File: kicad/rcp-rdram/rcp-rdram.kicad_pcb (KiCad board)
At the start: 2 copper layers, 47.1 x 49.7 mm, 32 parts, among them P1 RDRAM-EDGE, U11 RDRAM18-NUS, U11-2 RDRAM18-NUS, U14 RDRAM18-NUS, U14-2 RDRAM18-NUS, U15 MX8330, X2 14.705MHz

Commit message: Adjusted HC49 crystal to local footprint copy
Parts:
- X2: footprint Crystals:HC-49V -> n64:Crystal_HC-49V
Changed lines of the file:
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@@
       (net 2 GND) (zone_connect 1))
   )
-  (module Crystals:HC-49V (layer B.Cu)
+  (module n64:Crystal_HC-49V (layer B.Cu)
     (at 60.966 61.341 180)
     (descr "Quartz boitier HC-49 Vertical")

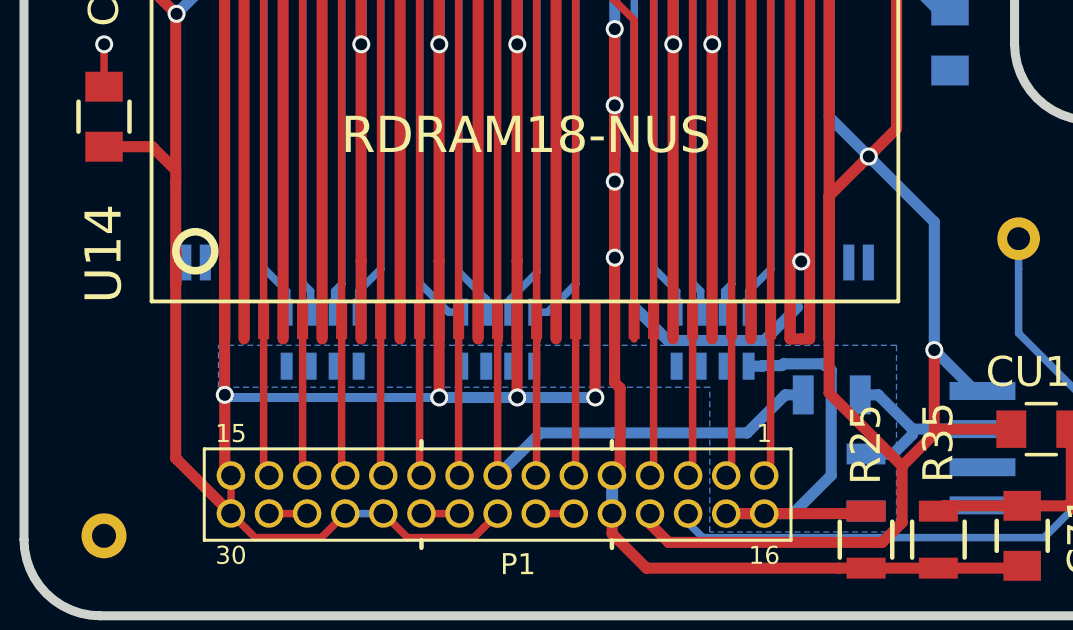
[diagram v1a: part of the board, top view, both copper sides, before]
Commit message: VTERM decouple capacitors added
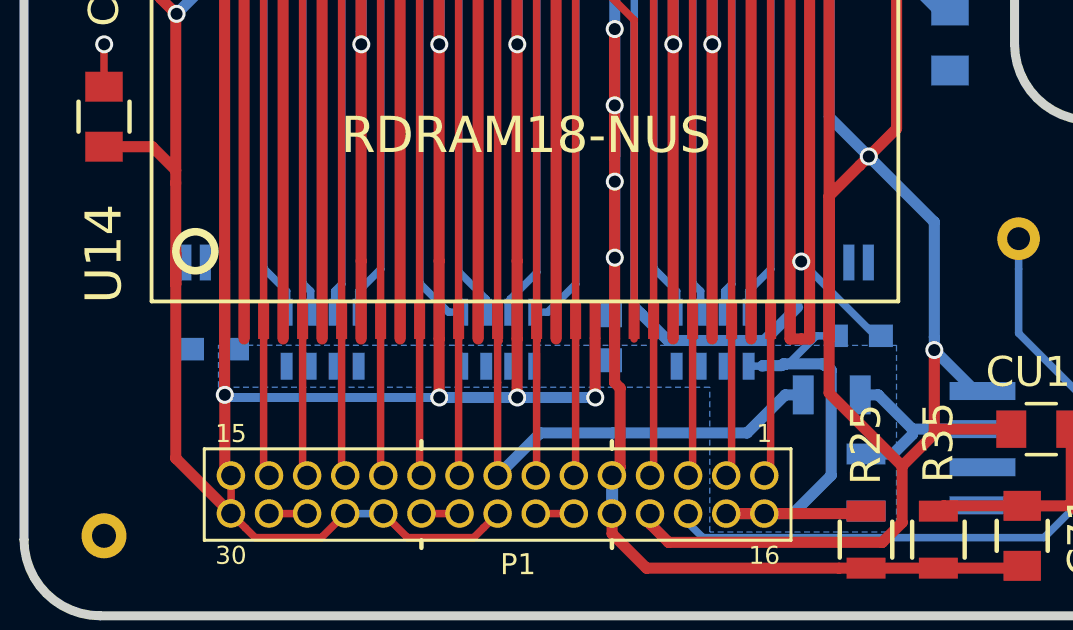
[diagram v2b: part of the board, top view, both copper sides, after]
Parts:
- added C1: 100nF, Capacitors_SMD:C_0603, B.Cu at (29.1, 65.0)
- added C2: 100nF, n64:C_0603, B.Cu at (42.3, 64.6)
- added C3: 100nF, n64:C_0603, B.Cu at (50.5, 64.6)
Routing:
- net GND: track 677.8 -> 681.4 mm
- net /VTERM: track 15.1 -> 18.0 mm
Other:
- board text added: "15"
- board text added: "30"
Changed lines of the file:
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@@
-(kicad_pcb (version 4) (host pcbnew 4.0.5)
+(kicad_pcb (version 4) (host pcbnew 4.0.6)
   (general
-    (links 203)
+    (links 209)
     (no_connects 0)
     (area 22.582999 24.105399 70.000001 74.062401)
     (thickness 1.6)
-    (drawings 25)
-    (tracks 606)
+    (drawings 27)
+    (tracks 612)
     (zones 0)
-    (modules 32)
+    (modules 35)
     (nets 28)
   )
@@
     (last_trace_width 0.25)
     (trace_clearance 0.2)
-    (zone_clearance 0.4)
+    (zone_clearance 0.508)
     (zone_45_only no)
     (trace_min 0.2)
@@
     (tags "resistor 0805")
     (attr smd)
-    (fp_text reference R33 (at 0.043 -1.548 180) (layer B.SilkS)
+    (fp_text reference R33 (at 2.159 0 270) (layer B.SilkS)
       (effects (font (size 0.7 0.7) (thickness 0.15)) (justify mirror))
     )
@@
       (rotate (xyz -90 0 0))
     )
+  )
+  (module Capacitors_SMD:C_0603 (layer B.Cu)
+    (at 29.083 65.024)
+    (descr "Capacitor SMD 0603, reflow soldering, AVX (see smccp.pdf)")
+    (tags "capacitor 0603")
+    (attr smd)
+    (fp_text reference C1 (at -1.27 1.3335) (layer B.SilkS)
+      (effects (font (size 0.7 0.7) (thickness 0.15)) (justify mirror))
+    )
+    (fp_text value 100nF (at 0 -1.5) (layer B.Fab)
+      (effects (font (size 1 1) (thickness 0.15)) (justify mirror))
+    )
+    (fp_line (start 1.4 -0.65) (end -1.4 -0.65) (layer B.CrtYd) (width 0.05))
+    (fp_line (start 1.4 -0.65) (end 1.4 0.65) (layer B.CrtYd) (width 0.05))
+    (fp_line (start -1.4 0.65) (end -1.4 -0.65) (layer B.CrtYd) (width 0.05))
+    (fp_line (start -1.4 0.65) (end 1.4 0.65) (layer B.CrtYd) (width 0.05))
+    (fp_line (start 0.35 -0.6) (end -0.35 -0.6) (layer B.SilkS) (width 0.12))
+    (fp_line (start -0.35 0.6) (end 0.35 0.6) (layer B.SilkS) (width 0.12))
+    (fp_line (start -0.8 0.4) (end 0.8 0.4) (layer B.Fab) (width 0.1))
+    (fp_line (start 0.8 0.4) (end 0.8 -0.4) (layer B.Fab) (width 0.1))
+    (fp_line (start 0.8 -0.4) (end -0.8 -0.4) (layer B.Fab) (width 0.1))
+    (fp_line (start -0.8 -0.4) (end -0.8 0.4) (layer B.Fab) (width 0.1))
+    (fp_text user %R (at 0 0) (layer B.Fab)
+      (effects (font (size 0.3 0.3) (thickness 0.075)) (justify mirror))
+    )
+    (pad 2 smd rect (at 0.75 0) (size 0.8 0.75) (layers B.Cu B.Paste B.Mask)
+      (net 20 /VTERM))
+    (pad 1 smd rect (at -0.75 0) (size 0.8 0.75) (layers B.Cu B.Paste B.Mask)
+      (net 2 GND))
+    (model Capacitors_SMD.3dshapes/C_0603.wrl
+      (at (xyz 0 0 0))
+      (scale (xyz 1 1 1))
+      (rotate (xyz 0 0 0))
+    )
+  )
+  (module n64:C_0603 (layer B.Cu)
+    (at 42.291 64.643 270)
+    (descr "Capacitor SMD 0603, reflow soldering, AVX (see smccp.pdf)")
+    (tags "capacitor 0603")
+    (attr smd)
+    (fp_text reference C2 (at 2.159 -0.508 270) (layer B.SilkS)
+      (effects (font (size 0.7 0.7) (thickness 0.15)) (justify mirror))
+    )
+    (fp_text value 100nF (at 0 -1.5 270) (layer B.Fab)
+      (effects (font (size 1 1) (thickness 0.15)) (justify mirror))
+    )
+    (fp_text user %R (at 0 1.5 270) (layer B.Fab)
+      (effects (font (size 1 1) (thickness 0.15)) (justify mirror))
+    )
+    (fp_line (start -0.8 -0.4) (end -0.8 0.4) (layer B.Fab) (width 0.1))
+    (fp_line (start 0.8 -0.4) (end -0.8 -0.4) (layer B.Fab) (width 0.1))
+    (fp_line (start 0.8 0.4) (end 0.8 -0.4) (layer B.Fab) (width 0.1))
+    (fp_line (start -0.8 0.4) (end 0.8 0.4) (layer B.Fab) (width 0.1))
+    (fp_line (start -0.35 0.6) (end 0.35 0.6) (layer B.SilkS) (width 0.12))
+    (fp_line (start 0.35 -0.6) (end -0.35 -0.6) (layer B.SilkS) (width 0.12))
+    (fp_line (start -1.4 0.65) (end 1.4 0.65) (layer B.CrtYd) (width 0.05))
+    (fp_line (start -1.4 0.65) (end -1.4 -0.65) (layer B.CrtYd) (width 0.05))
+    (fp_line (start 1.4 -0.65) (end 1.4 0.65) (layer B.CrtYd) (width 0.05))
+    (fp_line (start 1.4 -0.65) (end -1.4 -0.65) (layer B.CrtYd) (width 0.05))
+    (pad 1 smd rect (at -0.75 0 270) (size 0.8 0.75) (layers B.Cu B.Paste B.Mask)
+      (net 2 GND))
+    (pad 2 smd rect (at 0.75 0 270) (size 0.8 0.75) (layers B.Cu B.Paste B.Mask)
+      (net 20 /VTERM))
+    (model Capacitors_SMD.3dshapes/C_0603.wrl
+      (at (xyz 0 0 0))
+      (scale (xyz 1 1 1))
+      (rotate (xyz 0 0 0))
+    )
+  )
+  (module n64:C_0603 (layer B.Cu)
+    (at 50.546 64.5795 180)
+    (descr "Capacitor SMD 0603, reflow soldering, AVX (see smccp.pdf)")
+    (tags "capacitor 0603")
+    (attr smd)
+    (fp_text reference C3 (at -1.905 0.889 270) (layer B.SilkS)
+      (effects (font (size 0.7 0.7) (thickness 0.15)) (justify mirror))
+    )
+    (fp_text value 100nF (at 0 -1.5 180) (layer B.Fab)
+      (effects (font (size 1 1) (thickness 0.15)) (justify mirror))
+    )
+    (fp_text user %R (at 0 1.5 180) (layer B.Fab)
+      (effects (font (size 1 1) (thickness 0.15)) (justify mirror))
+    )
+    (fp_line (start -0.8 -0.4) (end -0.8 0.4) (layer B.Fab) (width 0.1))
+    (fp_line (start 0.8 -0.4) (end -0.8 -0.4) (layer B.Fab) (width 0.1))
+    (fp_line (start 0.8 0.4) (end 0.8 -0.4) (layer B.Fab) (width 0.1))
+    (fp_line (start -0.8 0.4) (end 0.8 0.4) (layer B.Fab) (width 0.1))
+    (fp_line (start -0.35 0.6) (end 0.35 0.6) (layer B.SilkS) (width 0.12))
+    (fp_line (start 0.35 -0.6) (end -0.35 -0.6) (layer B.SilkS) (width 0.12))
+    (fp_line (start -1.4 0.65) (end 1.4 0.65) (layer B.CrtYd) (width 0.05))
+    (fp_line (start -1.4 0.65) (end -1.4 -0.65) (layer B.CrtYd) (width 0.05))
+    (fp_line (start 1.4 -0.65) (end 1.4 0.65) (layer B.CrtYd) (width 0.05))
+    (fp_line (start 1.4 -0.65) (end -1.4 -0.65) (layer B.CrtYd) (width 0.05))
+    (pad 1 smd rect (at -0.75 0 180) (size 0.8 0.75) (layers B.Cu B.Paste B.Mask)
+      (net 2 GND))
+    (pad 2 smd rect (at 0.75 0 180) (size 0.8 0.75) (layers B.Cu B.Paste B.Mask)
+      (net 20 /VTERM))
+    (model Capacitors_SMD.3dshapes/C_0603.wrl
+      (at (xyz 0 0 0))
+      (scale (xyz 1 1 1))
+      (rotate (xyz 0 0 0))
+    )
+  )
+  (gr_text 15 (at 28.067 69.215) (layer B.SilkS)
+    (effects (font (size 0.6 0.6) (thickness 0.15)) (justify mirror))
+  )
+  (gr_text 30 (at 28.067 70.612) (layer B.SilkS)
+    (effects (font (size 0.6 0.6) (thickness 0.15)) (justify mirror))
   )
   (gr_circle (center 48.3235 68.3895) (end 48.3235 68.453) (layer B.SilkS) (width 0.2))
@@
   (segment (start 42.322384 70.513016) (end 42.33 70.5054) (width 0.37) (layer F.Cu) (net 1))
   (segment (start 42.42 69.1454) (end 42.33 69.2354) (width 0.25) (layer F.Cu) (net 1))
+  (segment (start 51.296 64.5795) (end 51.1175 64.5795) (width 0.25) (layer B.Cu) (net 2))
+  (segment (start 51.1175 64.5795) (end 48.940999 62.402999) (width 0.25) (layer B.Cu) (net 2))
+  (segment (start 48.940999 62.402999) (end 48.641 62.103) (width 0.25) (layer B.Cu) (net 2))
   (segment (start 39.796 70.5054) (end 41.066 70.5054) (width 0.25) (layer F.Cu) (net 2))
   (segment (start 35.986 70.5054) (end 37.256 70.5054) (width 0.25) (layer F.Cu) (net 2))
@@
   (segment (start 30.725999 49.085401) (end 30.726 49.0854) (width 0.25) (layer B.Cu) (net 19))
   (segment (start 30.719999 64.685401) (end 30.719999 47.1354) (width 0.25) (layer F.Cu) (net 19))
-  (segment (start 46.888722 65.591848) (end 47.338722 65.591848) (width 0.37) (layer B.Cu) (net 20))
+  (segment (start 49.796 64.5795) (end 49.146 64.5795) (width 0.25) (layer B.Cu) (net 20))
+  (segment (start 49.146 64.5795) (end 48.133652 65.591848) (width 0.25) (layer B.Cu) (net 20))
+  (segment (start 48.133652 65.591848) (end 47.338722 65.591848) (width 0.25) (layer B.Cu) (net 20))
+  (segment (start 47.338722 65.591848) (end 46.888722 65.591848) (width 0.25) (layer B.Cu) (net 20))
   (segment (start 48.048999 65.512999) (end 49.365001 65.512999) (width 0.37) (layer B.Cu) (net 20))
   (segment (start 47.338722 65.591848) (end 47.357571 65.572999) (width 0.37) (layer B.Cu) (net 20))
@@
     (connect_pads (clearance 0.508))
     (min_thickness 0.254)
-    (fill yes (arc_segments 32) (thermal_gap 0.3) (thermal_bridge_width 0.35))
+    (fill yes (arc_segments 32) (thermal_gap 0.25) (thermal_bridge_width 0.35))
     (polygon
       (pts

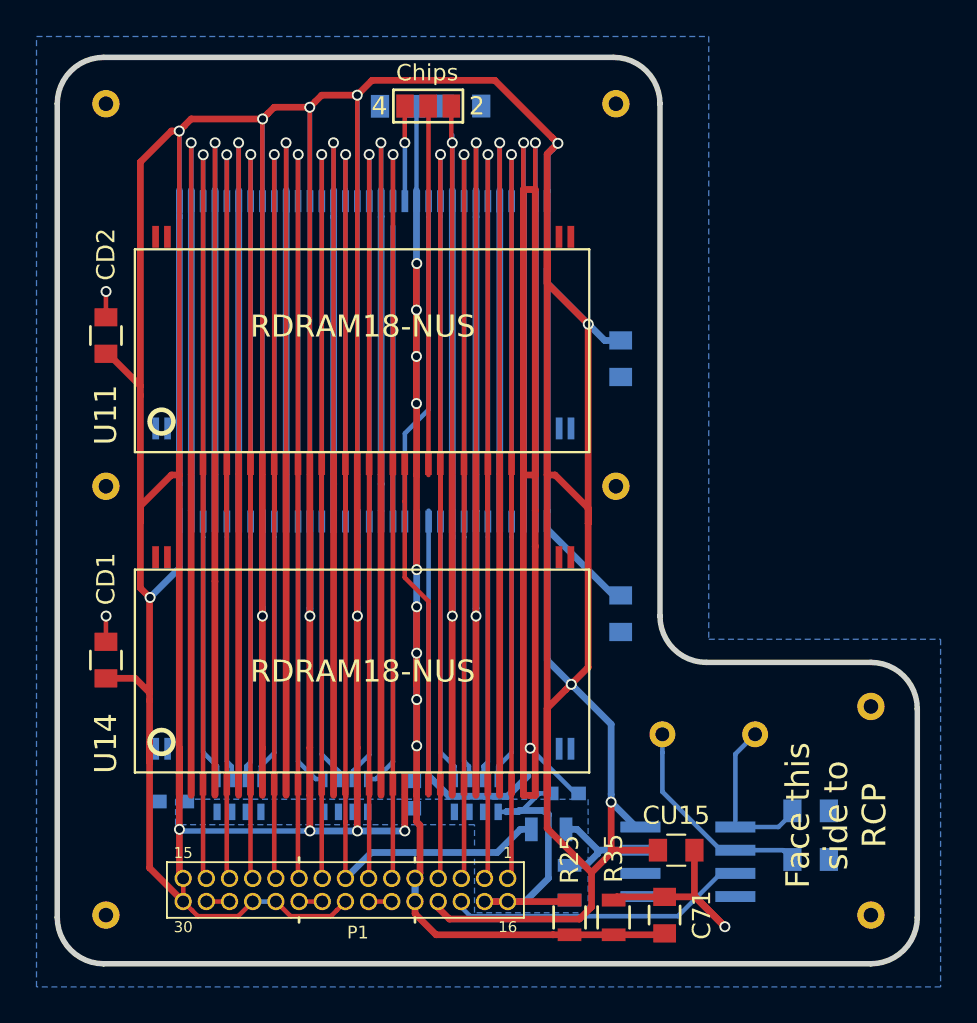
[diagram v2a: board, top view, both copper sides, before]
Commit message: Newer version according to modified schematics, need slight updates on Silk Screen
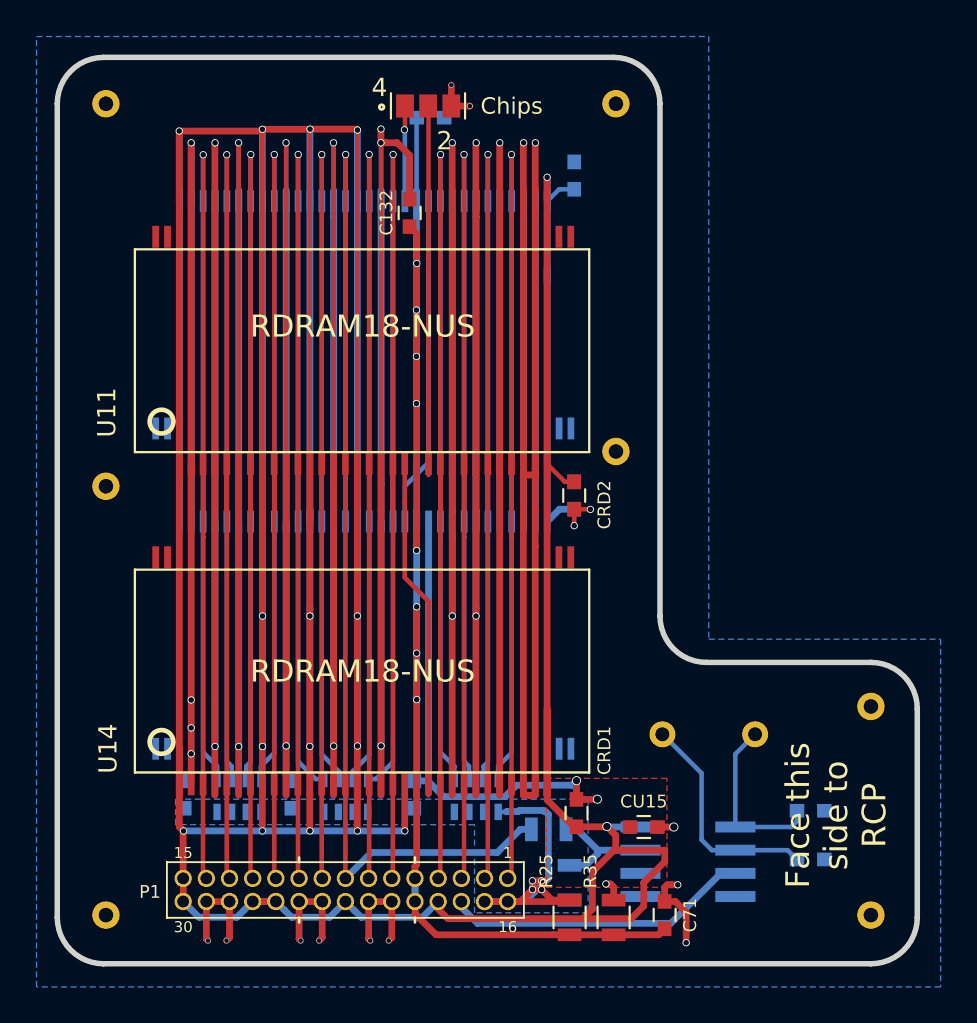
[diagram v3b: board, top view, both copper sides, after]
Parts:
- removed C1: 100nF, Capacitors_SMD:C_0603
- removed C2, C3: 100nF, n64:C_0603
- removed CD1, CD2, CD3, CD4: 10uF, Capacitors_SMD:C_0805
- added CRD1: .1uF, n64:C_0603, F.Cu at (51.2, 65.7)
- added CRD2: .1uF, n64:C_0603, F.Cu at (51.1, 48.3)
- added CRD3: .1uF, n64:C_0603, B.Cu at (51.1, 30.7)
- added CRD4: .1uF, n64:C_0603, B.Cu at (51.1, 48.3)
- added CVT1: .1uF, n64:C_0603, B.Cu at (42.3, 64.6)
- added CVT2: .1uF, n64:C_0603, B.Cu at (35.6, 64.6)
- added CVT3: .1uF, n64:C_0603, B.Cu at (29.7, 64.6)
- C132: footprint Capacitors_SMD:C_0805 -> n64:C_0603; moved to F.Cu
- C133, C146, C147, C71: footprint Capacitors_SMD:C_0805 -> n64:C_0603
- CU15: value 10uF -> .1uF; footprint Capacitors_SMD:C_0805 -> n64:C_0603
- JP1: footprint Connectors:GS3 -> n64:Connectors_GS3
- R25: value 130 -> 130R; footprint Resistors_SMD:R_0805 -> n64:R_0805
- R32, R33: footprint Resistors_SMD:R_0805 -> n64:R_0805
- R35: value 390 -> 390R; footprint Resistors_SMD:R_0805 -> n64:R_0805
- moved C132 5.87 mm to (42.0, 32.8), turned to 90 degrees
- moved CU15 2.18 mm to (54.9, 66.4), turned to 180 degrees
- moved REF** 1.91 mm to (53.3, 45.8)
- moved C133 1.89 mm to (43.2, 27.6)
- moved JP1 1.28 mm to (41.8, 27.0), turned to 0 degrees
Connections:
- CU15 pad 1: VDD -> GND
- CU15 pad 2: GND -> +3V3
- P1 pad 15: VDD -> +3V3
- P1 pad 19: VDD -> +3V3
- P1 pad 23: VDD -> +3V3
- P1 pad 26: VDD -> +3V3
- P1 pad 27: VDD -> +3V3
- P1 pad 30: VDD -> +3V3
- U11 pad 1: VDD -> +3V3
- U11 pad 12: VDD -> +3V3
- U11 pad 16: VDD -> +3V3
- U11 pad 32: VDD -> +3V3
- U11 pad 8: VDD -> +3V3
- U11-2 pad 1: VDD -> +3V3
- U11-2 pad 12: VDD -> +3V3
- U11-2 pad 16: VDD -> +3V3
- U11-2 pad 32: VDD -> +3V3
- U11-2 pad 8: VDD -> +3V3
- U14 pad 1: VDD -> +3V3
- U14 pad 12: VDD -> +3V3
- U14 pad 16: VDD -> +3V3
- U14 pad 20: VDD -> +3V3
- U14 pad 32: VDD -> +3V3
- U14 pad 8: VDD -> +3V3
- U14-2 pad 1: VDD -> +3V3
- U14-2 pad 12: VDD -> +3V3
- U14-2 pad 16: VDD -> +3V3
- U14-2 pad 32: VDD -> +3V3
- U14-2 pad 8: VDD -> +3V3
- U15 pad 1: Net-(U15-Pad1) -> (no net)
- U15 pad 4: VDD -> +3V3
- U15 pad 8: Net-(U15-Pad8) -> (no net)
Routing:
- net VDD: track 527.5 -> 0.00 mm, vias 16 -> 0
- net +3V3: track 0.00 -> 428.1 mm, vias 0 -> 17
- net GND: track 681.4 -> 756.1 mm, vias 17 -> 38
- net /VREF: track 81.8 -> 76.7 mm, vias 9 -> 8
- net /VTERM: track 18.0 -> 20.5 mm, vias 0 -> 4
- net Net-(JP1-Pad1): track 4.66 -> 5.25 mm
- net Net-(C146-Pad1): track 11.8 -> 12.4 mm
- net Net-(C147-Pad1): track 9.09 -> 9.61 mm
- added copper zone on F.Cu, net +3V3
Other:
- net class Default: via_dia 0.6 -> 0.3; via_drill 0.4 -> 0.25
- net class PWR added: clearance 0.2, trace_width 0.37, via_dia 0.4, via_drill 0.3
- rule via_min_drill: 0.3 -> 0.2
- rule via_min_size: 0.4 -> 0.3
- board text added: "N64 RAM board v.4"
- board text removed: "N64 RAM board v.3"

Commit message: Re-routing for 4 layer PCB
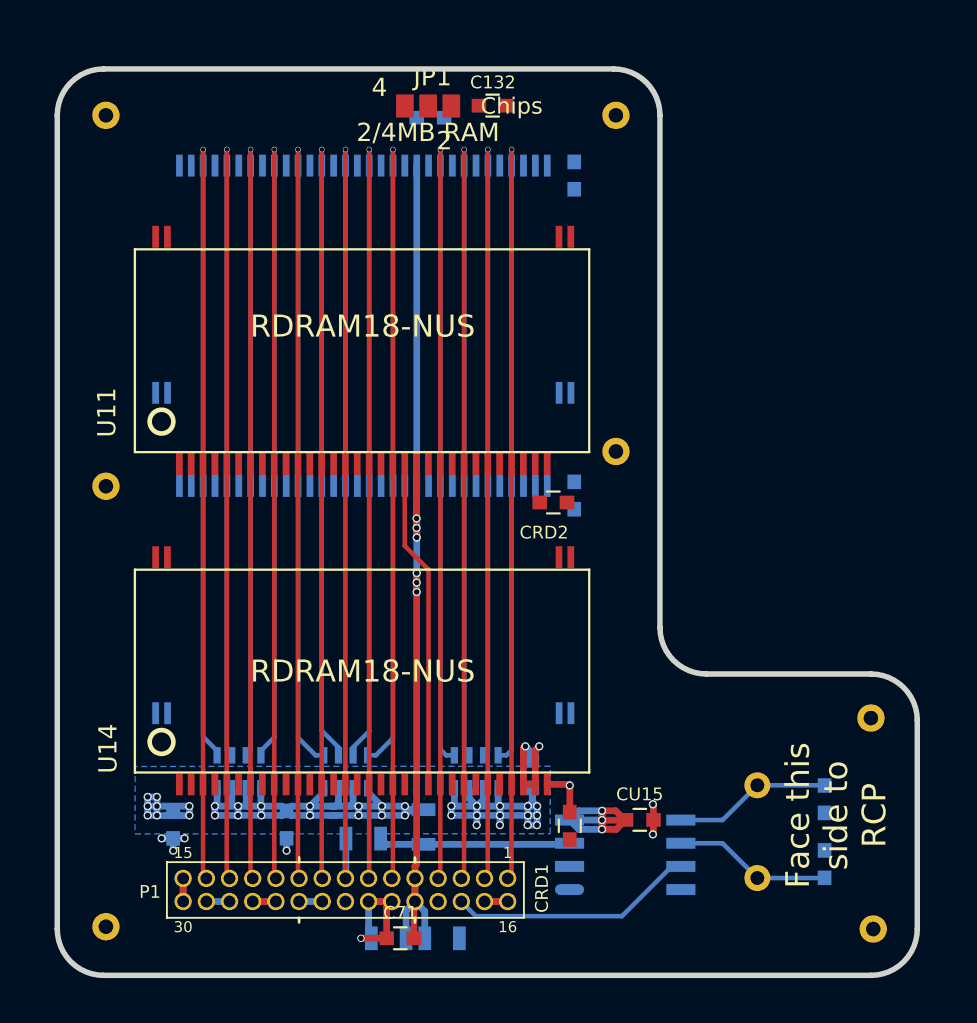
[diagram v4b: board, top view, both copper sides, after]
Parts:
- JP1: footprint n64:Connectors_GS3 -> n64:SolderPoint_3P
- R25, R35: moved to B.Cu
- U15: value MX8330 -> 8330; footprint n64:so-08 -> n64:mx8330-sop-8
- moved C71 14.5 mm to (41.5, 72.5), turned to 180 degrees
- moved R35 12.4 mm to (40.9, 72.5), turned to 180 degrees
- moved R33 10.2 mm to (39.5, 67.1)
- moved R32 8.56 mm to (42.8, 66.4), turned to 90 degrees
- moved C132 7.43 mm to (46.6, 26.9), turned to 0 degrees
- moved R25 7.08 mm to (43.8, 72.5), turned to 180 degrees
- moved CVT1 6.56 mm to (48.8, 63.5)
- moved U15 3.46 mm to (53.8, 67.9), turned to 0 degrees
- moved X2 2.80 mm to (61.1, 64.1), turned to 270 degrees
- moved U14-2 1.95 mm to (39.5, 35.5)
- moved U11-2 1.95 mm to (39.5, 53.1)
- moved CVT3 1.77 mm to (29.1, 66.3), turned to 90 degrees
- moved CVT2 1.67 mm to (35.3, 66.3), turned to 90 degrees
- moved RA1 1.30 mm to (32.7, 63.4)
- moved RA2 1.30 mm to (38.5, 63.4)
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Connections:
- U15 pad 1: (no net) -> Net-(U15-Pad1)
- U15 pad 8: (no net) -> Net-(U15-Pad8)
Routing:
- net GND: track 756.1 -> 22.0 mm, vias 38 -> 9
- net +3V3: track 428.1 -> 22.4 mm, vias 17 -> 4
- net /VTERM: track 20.5 -> 69.8 mm, vias 4 -> 36
- net /VREF: track 76.7 -> 54.7 mm, vias 8 -> 6
- net Net-(JP1-Pad2): track 20.2 -> 0.00 mm
- net /COMMAND: track 92.3 -> 74.0 mm
- net Net-(U11-2-Pad20): track 18.1 -> 0.00 mm
- net /TXCLK: track 72.5 -> 60.8 mm
- net Net-(JP1-Pad1): track 5.25 -> 0.00 mm, vias 1 -> 0
- net Net-(R32-Pad1): track 6.55 -> 10.5 mm
- net Net-(C146-Pad1): track 12.4 -> 8.67 mm
- net /ENABLE: track 16.8 -> 13.5 mm
- net /DQ7: track 76.3 -> 73.3 mm
- net /DQ4: track 76.2 -> 73.5 mm
- net /ADDRESS: track 76.0 -> 73.3 mm
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- added copper zone on Pwr.Cu, net +3V3
- added copper zone on Pwr.Cu, net /VTERM
- added copper zone on Gnd.Cu, net GND
- removed copper zone on F.Cu, net +3V3
- removed copper zone on B.Cu, net GND
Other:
- copper layers 2 -> 4
- net class PWR: via_dia 0.4 -> 0.45
